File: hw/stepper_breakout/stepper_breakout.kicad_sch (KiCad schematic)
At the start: 7 parts, among them J1 Conn_01x02_Pin, U1 Teensy4.1

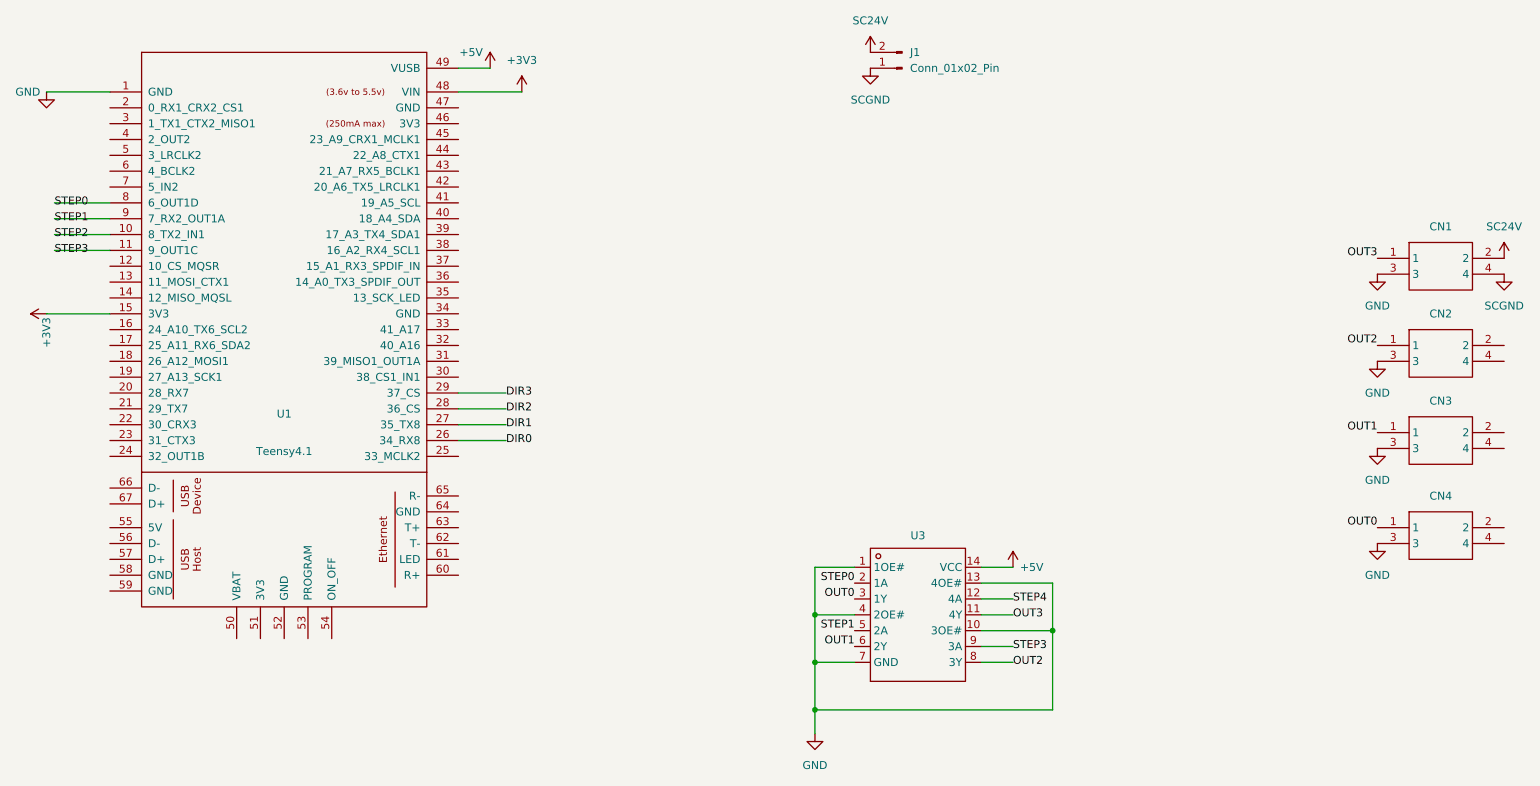
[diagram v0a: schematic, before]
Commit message: Schematic + routing for teensy breakout
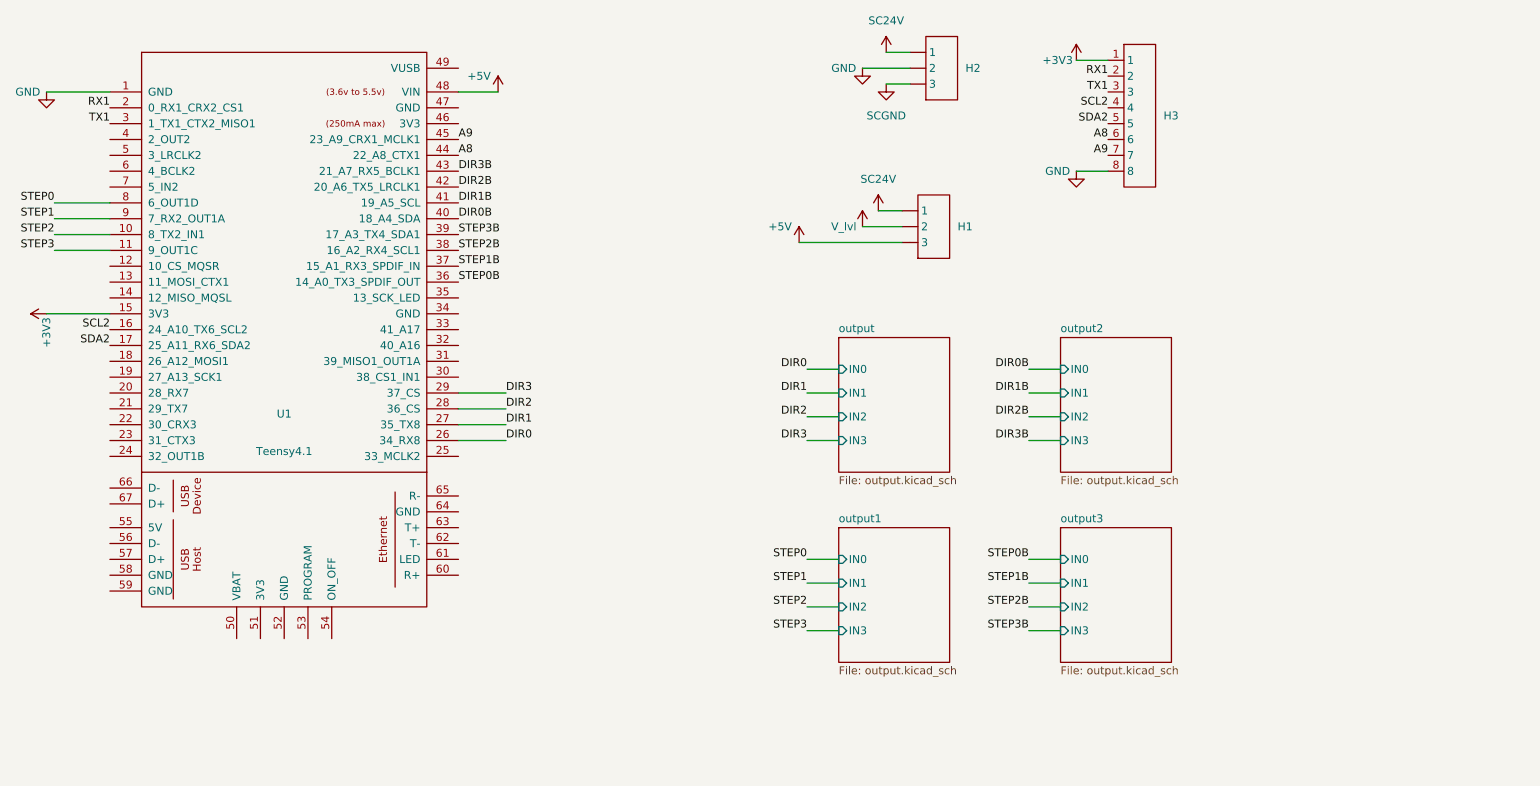
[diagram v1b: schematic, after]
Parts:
- removed CN1, CN2, CN3, CN4: (no value), EasyEDA_Lib:CONN-TH_HAA420A-4A, symbol EasyEDA_Lib:pitch4.2MMsocket2*2P
- removed J1: Conn_01x02_Pin, Connector_PinHeader_2.54mm:PinHeader_1x02_P2.54mm_Vertical, symbol Connector:Conn_01x02_Pin
- removed U3: (no value), EasyEDA_Lib:SOIC-14_L8.7-W3.9-P1.27-LS6.0-BL, symbol EasyEDA_Lib:SN74AHCT125DR
- added H1, H2: (no value), EasyEDA_Lib:HDR-TH_3P-P2.54-V-M-1, symbol EasyEDA_Lib:Header-Male-2.54_1x3
- added H3: (no value), EasyEDA_Lib:HDR-TH_8P-P2.54-V-M, symbol EasyEDA_Lib:KH-2.54PH180-1X8P-L11.5
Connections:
- net +3V3: now also H3.1; no longer U1.48 (VIN)
- net +5V: now also U1.48 (VIN), H1.3; no longer U1.49 (VUSB)
- net GND: now also H2.2, H3.8
- net SC24V: now also H1.1, H2.1
- net SCGND: now also H2.3
- net SCL2: now reaches U1.16 (24_A10_TX6_SCL2)
- net SCL2: now also H3.4
- net SDA2: now reaches U1.17 (25_A11_RX6_SDA2)
- net SDA2: now also H3.5
- net RX1: now reaches U1.2 (0_RX1_CRX2_CS1)
- net RX1: now also H3.2
- net TX1: now reaches U1.3 (1_TX1_CTX2_MISO1)
- net TX1: now also H3.3
- net STEP0B: now reaches U1.36 (14_A0_TX3_SPDIF_OUT)
- net STEP1B: now reaches U1.37 (15_A1_RX3_SPDIF_IN)
- net STEP2B: now reaches U1.38 (16_A2_RX4_SCL1)
- net STEP3B: now reaches U1.39 (17_A3_TX4_SDA1)
- net DIR0B: now reaches U1.40 (18_A4_SDA)
- net DIR1B: now reaches U1.41 (19_A5_SCL)
- net DIR2B: now reaches U1.42 (20_A6_TX5_LRCLK1)
- net DIR3B: now reaches U1.43 (21_A7_RX5_BCLK1)
- net A8: now reaches U1.44 (22_A8_CTX1)
- net A8: now also H3.6
- net A9: now reaches U1.45 (23_A9_CRX1_MCLK1)
- net A9: now also H3.7
- new net V_lvl: H1.2
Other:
- added sheet output (output.kicad_sch)
- added sheet output1 (output.kicad_sch)
- added sheet output2 (output.kicad_sch)
- added sheet output3 (output.kicad_sch)

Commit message: Added test mode
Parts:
- H1, H2: LCSC (none) -> C49257; Supplier Part C49257 -> (none)
- H3: LCSC (none) -> C2905487; Supplier Part C2905487 -> (none)
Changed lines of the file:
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@@
 			)
 		)
-		(property "Supplier Part" "C49257"
+		(property "LCSC" "C49257"
 			(at 180.34 43.18 0)
 			(hide yes)
@@
 			)
 		)
-		(property "Supplier Part" "C49257"
+		(property "LCSC" "C49257"
 			(at 179.07 68.58 0)
 			(hide yes)
@@
 			)
 		)
-		(property "Supplier Part" "C2905487"
-			(at 213.36 50.8 0)
-			(hide yes)
+		(property "LCSC" "C2905487"
+			(at 213.36 50.8 0)
+			(hide yes)
